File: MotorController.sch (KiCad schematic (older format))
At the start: 0 parts

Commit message: Added power, touch, and motor controller
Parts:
- added C? (x2): .1uF, symbol C
- added C? (x2): C, symbol C
- added M? (x4): Motor_DC, symbol Motor_DC
- added R? (x6): 10k, symbol R
- added U? (x2): A3916, symbol A3916
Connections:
- new net: M?.2 (-), U?.10 (OUT2B) (x2)
- new net: M?.2 (-), U?.12 (OUT1B) (x2)
- new net: R?.2, U?.13 (SENSE1) (x2)
- new net: M?.1 (+), U?.14 (OUT1A) (x2)
- new net: C?.1, U?.15 (VCP) (x2)
- new net: R?.1, U?.7 (FAULTn) (x2)
- new net: M?.1 (+), U?.8 (OUT2A) (x2)
- new net: R?.2, U?.9 (SENSE2) (x2)
- new net +5V: R?.2, R?.2
- new net 3V7: C?.1, C?.1, C?.2, C?.2, U?.11 (VBB), U?.11 (VBB)
- new net GND: C?.2, C?.2, R?.1, R?.1, R?.1, R?.1, U?.1 (GND), U?.1 (GND)
- new net MC1_IN1: U?.3 (IN1)
- new net MC1_IN2: U?.4 (IN2)
- new net MC1_IN3: U?.5 (IN3)
- new net MC1_IN4: U?.6 (IN4)
- new net MC1_SLEEPn: U?.2 (SLEEPn)
- new net MC2_IN1: U?.3 (IN1)
- new net MC2_IN2: U?.4 (IN2)
- new net MC2_IN3: U?.5 (IN3)
- new net MC2_IN4: U?.6 (IN4)
- new net MC2_SLEEPn: U?.2 (SLEEPn)

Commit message: Adding IR Sensor
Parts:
- gave numbers to parts that had none: 16
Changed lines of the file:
@@
 $EndDescr
 $Comp
-L A3916 U?
+L A3916 U1
 U 1 1 5AA4F077
 P 3775 3850
-F 0 "U?" H 3775 3750 60  0000 C CNN
+F 0 "U1" H 3775 3750 60  0000 C CNN
 F 1 "A3916" H 3775 3950 60  0000 C CNN
 F 2 "" H 3775 3850 60  0001 C CNN
@@
 MC1_IN4
 $Comp
-L R R?
+L R R1
 U 1 1 5AA4F12C
 P 2925 4100
-F 0 "R?" V 3005 4100 50  0000 C CNN
+F 0 "R1" V 3005 4100 50  0000 C CNN
 F 1 "10k" V 2925 4100 50  0000 C CNN
 F 2 "" V 2855 4100 50  0001 C CNN
@@
 $EndComp
 $Comp
-L +5V #PWR?
+L +5V #PWR01
 U 1 1 5AA4F16D
 P 2475 4100
-F 0 "#PWR?" H 2475 3950 50  0001 C CNN
+F 0 "#PWR01" H 2475 3950 50  0001 C CNN
 F 1 "+5V" H 2475 4240 50  0000 C CNN
 F 2 "" H 2475 4100 50  0001 C CNN
@@
 	2475 4100 2775 4100
 $Comp
-L GND #PWR?
+L GND #PWR02
 U 1 1 5AA4F189
 P 3075 4200
-F 0 "#PWR?" H 3075 3950 50  0001 C CNN
+F 0 "#PWR02" H 3075 3950 50  0001 C CNN
 F 1 "GND" H 3075 4050 50  0000 C CNN
 F 2 "" H 3075 4200 50  0001 C CNN
@@
 $EndComp
 $Comp
-L C C?
+L C C1
 U 1 1 5AA4F1A9
 P 4675 3450
-F 0 "C?" H 4700 3550 50  0000 L CNN
+F 0 "C1" H 4700 3550 50  0000 L CNN
 F 1 ".1uF" H 4700 3350 50  0000 L CNN
 F 2 "" H 4713 3300 50  0001 C CNN
@@
 Connection ~ 4675 3600
 $Comp
-L C C?
+L C C2
 U 1 1 5AA5030C
 P 5100 3450
-F 0 "C?" H 5125 3550 50  0000 L CNN
+F 0 "C2" H 5125 3550 50  0000 L CNN
 F 1 "C" H 5125 3350 50  0000 L CNN
 F 2 "" H 5138 3300 50  0001 C CNN
@@
 $EndComp
 $Comp
-L GND #PWR?
+L GND #PWR03
 U 1 1 5AA5037F
 P 5325 3300
-F 0 "#PWR?" H 5325 3050 50  0001 C CNN
+F 0 "#PWR03" H 5325 3050 50  0001 C CNN
 F 1 "GND" H 5325 3150 50  0000 C CNN
 F 2 "" H 5325 3300 50  0001 C CNN
@@
 	5100 3300 5325 3300
 $Comp
-L Motor_DC M?
+L Motor_DC M1
 U 1 1 5AA50637
 P 5100 3900
-F 0 "M?" H 5200 4000 50  0000 L CNN
+F 0 "M1" H 5200 4000 50  0000 L CNN
 F 1 "Motor_DC" H 5200 3700 50  0000 L TNN
 F 2 "" H 5100 3810 50  0001 C CNN
@@
 $EndComp
 $Comp
-L Motor_DC M?
+L Motor_DC M2
 U 1 1 5AA506D8
 P 5100 4500
-F 0 "M?" H 5200 4600 50  0000 L CNN
+F 0 "M2" H 5200 4600 50  0000 L CNN
 F 1 "Motor_DC" H 5200 4300 50  0000 L TNN
 F 2 "" H 5100 4410 50  0001 C CNN
@@
 	4900 4200 5100 4200
 $Comp
-L R R?
+L R R3
 U 1 1 5AA50734
 P 4625 3900
-F 0 "R?" V 4705 3900 50  0000 C CNN
+F 0 "R3" V 4705 3900 50  0000 C CNN
 F 1 "10k" V 4625 3900 50  0000 C CNN
 F 2 "" V 4555 3900 50  0001 C CNN
@@
 $EndComp
 $Comp
-L GND #PWR?
+L GND #PWR04
 U 1 1 5AA5078D
 P 4775 3900
-F 0 "#PWR?" H 4775 3650 50  0001 C CNN
+F 0 "#PWR04" H 4775 3650 50  0001 C CNN
 F 1 "GND" H 4775 3750 50  0000 C CNN
 F 2 "" H 4775 3900 50  0001 C CNN
@@
 	4625 4800 5100 4800
 $Comp
-L R R?
+L R R2
 U 1 1 5AA507E1
 P 4475 4350
-F 0 "R?" V 4555 4350 50  0000 C CNN
+F 0 "R2" V 4555 4350 50  0000 C CNN
 F 1 "10k" V 4475 4350 50  0000 C CNN
 F 2 "" V 4405 4350 50  0001 C CNN
@@
 $EndComp
 $Comp
-L GND #PWR?
+L GND #PWR05
 U 1 1 5AA5082F
 P 4475 4500
-F 0 "#PWR?" H 4475 4250 50  0001 C CNN
+F 0 "#PWR05" H 4475 4250 50  0001 C CNN
 F 1 "GND" H 4475 4350 50  0000 C CNN
 F 2 "" H 4475 4500 50  0001 C CNN
@@
 $EndComp
 $Comp
-L A3916 U?
+L A3916 U2
 U 1 1 5AA50C8A
 P 7625 3825
-F 0 "U?" H 7625 3725 60  0000 C CNN
+F 0 "U2" H 7625 3725 60  0000 C CNN
 F 1 "A3916" H 7625 3925 60  0000 C CNN
 F 2 "" H 7625 3825 60  0001 C CNN
@@
 MC2_IN4
 $Comp
-L R R?
+L R R4
 U 1 1 5AA50C95
 P 6775 4075
-F 0 "R?" V 6855 4075 50  0000 C CNN
+F 0 "R4" V 6855 4075 50  0000 C CNN
 F 1 "10k" V 6775 4075 50  0000 C CNN
 F 2 "" V 6705 4075 50  0001 C CNN
@@
 $EndComp
 $Comp
-L +5V #PWR?
+L +5V #PWR06
 U 1 1 5AA50C9B
 P 6325 4075
-F 0 "#PWR?" H 6325 3925 50  0001 C CNN
+F 0 "#PWR06" H 6325 3925 50  0001 C CNN
 F 1 "+5V" H 6325 4215 50  0000 C CNN
 F 2 "" H 6325 4075 50  0001 C CNN
@@
 	6325 4075 6625 4075
 $Comp
-L GND #PWR?
+L GND #PWR07
 U 1 1 5AA50CA2
 P 6925 4175
-F 0 "#PWR?" H 6925 3925 50  0001 C CNN
+F 0 "#PWR07" H 6925 3925 50  0001 C CNN
 F 1 "GND" H 6925 4025 50  0000 C CNN
 F 2 "" H 6925 4175 50  0001 C CNN
@@
 $EndComp
 $Comp
-L C C?
+L C C3
 U 1 1 5AA50CA8
 P 8525 3425
-F 0 "C?" H 8550 3525 50  0000 L CNN
+F 0 "C3" H 8550 3525 50  0000 L CNN
 F 1 ".1uF" H 8550 3325 50  0000 L CNN
 F 2 "" H 8563 3275 50  0001 C CNN
@@
 Connection ~ 8525 3575
 $Comp
-L C C?
+L C C4
 U 1 1 5AA50CB2
 P 8950 3425
-F 0 "C?" H 8975 3525 50  0000 L CNN
+F 0 "C4" H 8975 3525 50  0000 L CNN
 F 1 "C" H 8975 3325 50  0000 L CNN
 F 2 "" H 8988 3275 50  0001 C CNN
@@
 $EndComp
 $Comp
-L GND #PWR?
+L GND #PWR08
 U 1 1 5AA50CB8
 P 9175 3275
-F 0 "#PWR?" H 9175 3025 50  0001 C CNN
+F 0 "#PWR08" H 9175 3025 50  0001 C CNN
 F 1 "GND" H 9175 3125 50  0000 C CNN
 F 2 "" H 9175 3275 50  0001 C CNN
@@
 	8950 3275 9175 3275
 $Comp
-L Motor_DC M?
+L Motor_DC M3
 U 1 1 5AA50CC1
 P 8950 3875
-F 0 "M?" H 9050 3975 50  0000 L CNN
+F 0 "M3" H 9050 3975 50  0000 L CNN
 F 1 "Motor_DC" H 9050 3675 50  0000 L TNN
 F 2 "" H 8950 3785 50  0001 C CNN
@@
 $EndComp
 $Comp
-L Motor_DC M?
+L Motor_DC M4
 U 1 1 5AA50CC7
 P 8950 4475
-F 0 "M?" H 9050 4575 50  0000 L CNN
+F 0 "M4" H 9050 4575 50  0000 L CNN
 F 1 "Motor_DC" H 9050 4275 50  0000 L TNN
 F 2 "" H 8950 4385 50  0001 C CNN
@@
 	8750 4175 8950 4175
 $Comp
-L R R?
+L R R6
 U 1 1 5AA50CD1
 P 8475 3875
-F 0 "R?" V 8555 3875 50  0000 C CNN
+F 0 "R6" V 8555 3875 50  0000 C CNN
 F 1 "10k" V 8475 3875 50  0000 C CNN
 F 2 "" V 8405 3875 50  0001 C CNN
@@
 $EndComp
 $Comp
-L GND #PWR?
+L GND #PWR09
 U 1 1 5AA50CD7
 P 8625 3875
-F 0 "#PWR?" H 8625 3625 50  0001 C CNN
+F 0 "#PWR09" H 8625 3625 50  0001 C CNN
 F 1 "GND" H 8625 3725 50  0000 C CNN
 F 2 "" H 8625 3875 50  0001 C CNN
@@
 	8475 4775 8950 4775
 $Comp
-L R R?
+L R R5
 U 1 1 5AA50CE3
 P 8325 4325
-F 0 "R?" V 8405 4325 50  0000 C CNN
+F 0 "R5" V 8405 4325 50  0000 C CNN
 F 1 "10k" V 8325 4325 50  0000 C CNN
 F 2 "" V 8255 4325 50  0001 C CNN
@@
 $EndComp
 $Comp
-L GND #PWR?
+L GND #PWR010
 U 1 1 5AA50CE9
 P 8325 4475
-F 0 "#PWR?" H 8325 4225 50  0001 C CNN
+F 0 "#PWR010" H 8325 4225 50  0001 C CNN
 F 1 "GND" H 8325 4325 50  0000 C CNN
 F 2 "" H 8325 4475 50  0001 C CNN

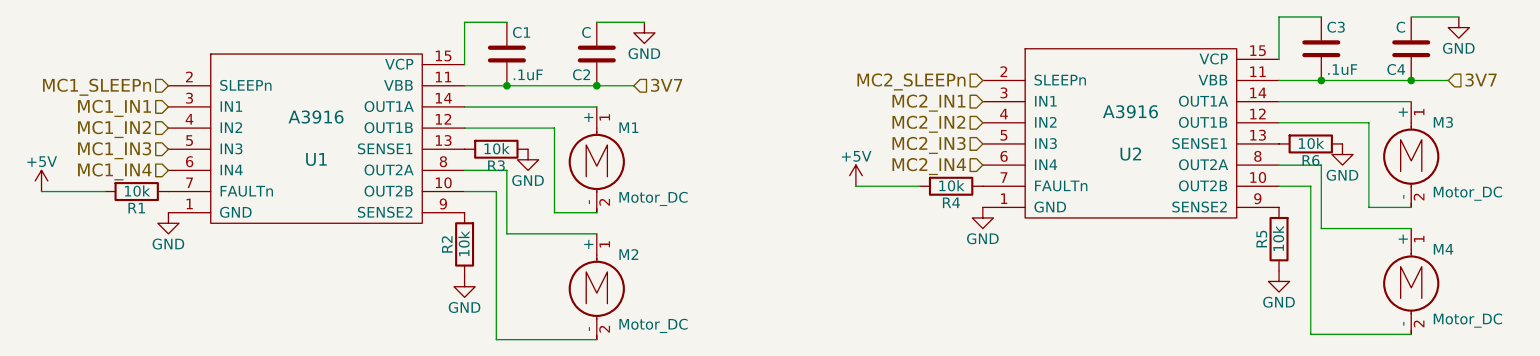
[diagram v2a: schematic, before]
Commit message: Started associating footprints
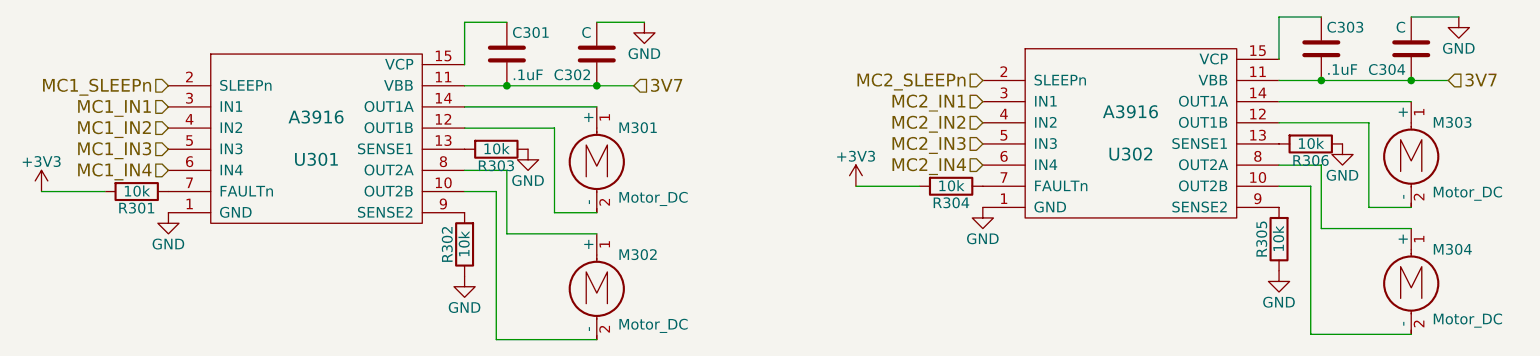
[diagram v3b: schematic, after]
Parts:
- C301: renamed from C1; footprint (none) -> Capacitors_SMD:C_0402
- C303: renamed from C3; footprint (none) -> Capacitors_SMD:C_0402
- renumbered C2 to C302, C4 to C304, M1 to M301, M2 to M302, M3 to M303, M4 to M304, R1 to R301, R2 to R302, R3 to R303, R4 to R304, R5 to R305, R6 to R306, U1 to U301, U2 to U302
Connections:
- net +5V renamed +3V3
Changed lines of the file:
@@
 $EndDescr
 $Comp
-L A3916 U1
+L A3916 U301
 U 1 1 5AA4F077
 P 3775 3850
-F 0 "U1" H 3775 3750 60  0000 C CNN
+F 0 "U301" H 3775 3750 60  0000 C CNN
 F 1 "A3916" H 3775 3950 60  0000 C CNN
 F 2 "" H 3775 3850 60  0001 C CNN
@@
 MC1_IN4
 $Comp
-L R R1
+L R R301
 U 1 1 5AA4F12C
 P 2925 4100
-F 0 "R1" V 3005 4100 50  0000 C CNN
+F 0 "R301" V 3005 4100 50  0000 C CNN
 F 1 "10k" V 2925 4100 50  0000 C CNN
 F 2 "" V 2855 4100 50  0001 C CNN
@@
 	0    1    1    0
 $EndComp
-$Comp
-L +5V #PWR01
-U 1 1 5AA4F16D
-P 2475 4100
-F 0 "#PWR01" H 2475 3950 50  0001 C CNN
-F 1 "+5V" H 2475 4240 50  0000 C CNN
-F 2 "" H 2475 4100 50  0001 C CNN
-F 3 "" H 2475 4100 50  0001 C CNN
-	1    2475 4100
-	1    0    0    -1
-$EndComp
 Wire Wire Line
 	2475 4100 2775 4100
 $Comp
-L GND #PWR02
+L GND #PWR013
 U 1 1 5AA4F189
 P 3075 4200
-F 0 "#PWR02" H 3075 3950 50  0001 C CNN
+F 0 "#PWR013" H 3075 3950 50  0001 C CNN
 F 1 "GND" H 3075 4050 50  0000 C CNN
 F 2 "" H 3075 4200 50  0001 C CNN
@@
 $EndComp
 $Comp
-L C C1
+L C C301
 U 1 1 5AA4F1A9
 P 4675 3450
-F 0 "C1" H 4700 3550 50  0000 L CNN
+F 0 "C301" H 4700 3550 50  0000 L CNN
 F 1 ".1uF" H 4700 3350 50  0000 L CNN
-F 2 "" H 4713 3300 50  0001 C CNN
+F 2 "Capacitors_SMD:C_0402" H 4713 3300 50  0001 C CNN
 F 3 "" H 4675 3450 50  0001 C CNN
 	1    4675 3450
@@
 Connection ~ 4675 3600
 $Comp
-L C C2
+L C C302
 U 1 1 5AA5030C
 P 5100 3450
-F 0 "C2" H 5125 3550 50  0000 L CNN
+F 0 "C302" H 5125 3550 50  0000 L CNN
 F 1 "C" H 5125 3350 50  0000 L CNN
 F 2 "" H 5138 3300 50  0001 C CNN
@@
 $EndComp
 $Comp
-L GND #PWR03
+L GND #PWR014
 U 1 1 5AA5037F
 P 5325 3300
-F 0 "#PWR03" H 5325 3050 50  0001 C CNN
+F 0 "#PWR014" H 5325 3050 50  0001 C CNN
 F 1 "GND" H 5325 3150 50  0000 C CNN
 F 2 "" H 5325 3300 50  0001 C CNN
@@
 	5100 3300 5325 3300
 $Comp
-L Motor_DC M1
+L Motor_DC M301
 U 1 1 5AA50637
 P 5100 3900
-F 0 "M1" H 5200 4000 50  0000 L CNN
+F 0 "M301" H 5200 4000 50  0000 L CNN
 F 1 "Motor_DC" H 5200 3700 50  0000 L TNN
 F 2 "" H 5100 3810 50  0001 C CNN
@@
 $EndComp
 $Comp
-L Motor_DC M2
+L Motor_DC M302
 U 1 1 5AA506D8
 P 5100 4500
-F 0 "M2" H 5200 4600 50  0000 L CNN
+F 0 "M302" H 5200 4600 50  0000 L CNN
 F 1 "Motor_DC" H 5200 4300 50  0000 L TNN
 F 2 "" H 5100 4410 50  0001 C CNN
@@
 	4900 4200 5100 4200
 $Comp
-L R R3
+L R R303
 U 1 1 5AA50734
 P 4625 3900
-F 0 "R3" V 4705 3900 50  0000 C CNN
+F 0 "R303" V 4705 3900 50  0000 C CNN
 F 1 "10k" V 4625 3900 50  0000 C CNN
 F 2 "" V 4555 3900 50  0001 C CNN
@@
 $EndComp
 $Comp
-L GND #PWR04
+L GND #PWR015
 U 1 1 5AA5078D
 P 4775 3900
-F 0 "#PWR04" H 4775 3650 50  0001 C CNN
+F 0 "#PWR015" H 4775 3650 50  0001 C CNN
 F 1 "GND" H 4775 3750 50  0000 C CNN
 F 2 "" H 4775 3900 50  0001 C CNN
@@
 	4625 4800 5100 4800
 $Comp
-L R R2
+L R R302
 U 1 1 5AA507E1
 P 4475 4350
-F 0 "R2" V 4555 4350 50  0000 C CNN
+F 0 "R302" V 4555 4350 50  0000 C CNN
 F 1 "10k" V 4475 4350 50  0000 C CNN
 F 2 "" V 4405 4350 50  0001 C CNN
@@
 $EndComp
 $Comp
-L GND #PWR05
+L GND #PWR016
 U 1 1 5AA5082F
 P 4475 4500
-F 0 "#PWR05" H 4475 4250 50  0001 C CNN
+F 0 "#PWR016" H 4475 4250 50  0001 C CNN
 F 1 "GND" H 4475 4350 50  0000 C CNN
 F 2 "" H 4475 4500 50  0001 C CNN
@@
 $EndComp
 $Comp
-L A3916 U2
+L A3916 U302
 U 1 1 5AA50C8A
 P 7625 3825
-F 0 "U2" H 7625 3725 60  0000 C CNN
+F 0 "U302" H 7625 3725 60  0000 C CNN
 F 1 "A3916" H 7625 3925 60  0000 C CNN
 F 2 "" H 7625 3825 60  0001 C CNN
@@
 MC2_IN4
 $Comp
-L R R4
+L R R304
 U 1 1 5AA50C95
 P 6775 4075
-F 0 "R4" V 6855 4075 50  0000 C CNN
+F 0 "R304" V 6855 4075 50  0000 C CNN
 F 1 "10k" V 6775 4075 50  0000 C CNN
 F 2 "" V 6705 4075 50  0001 C CNN
@@
 	0    1    1    0
 $EndComp
-$Comp
-L +5V #PWR06
-U 1 1 5AA50C9B
-P 6325 4075
-F 0 "#PWR06" H 6325 3925 50  0001 C CNN
-F 1 "+5V" H 6325 4215 50  0000 C CNN
-F 2 "" H 6325 4075 50  0001 C CNN
-F 3 "" H 6325 4075 50  0001 C CNN
-	1    6325 4075
-	1    0    0    -1
-$EndComp
 Wire Wire Line
 	6325 4075 6625 4075
 $Comp
-L GND #PWR07
+L GND #PWR017
 U 1 1 5AA50CA2
 P 6925 4175
-F 0 "#PWR07" H 6925 3925 50  0001 C CNN
+F 0 "#PWR017" H 6925 3925 50  0001 C CNN
 F 1 "GND" H 6925 4025 50  0000 C CNN
 F 2 "" H 6925 4175 50  0001 C CNN
@@
 $EndComp
 $Comp
-L C C3
+L C C303
 U 1 1 5AA50CA8
 P 8525 3425
-F 0 "C3" H 8550 3525 50  0000 L CNN
+F 0 "C303" H 8550 3525 50  0000 L CNN
 F 1 ".1uF" H 8550 3325 50  0000 L CNN
-F 2 "" H 8563 3275 50  0001 C CNN
+F 2 "Capacitors_SMD:C_0402" H 8563 3275 50  0001 C CNN
 F 3 "" H 8525 3425 50  0001 C CNN
 	1    8525 3425
@@
 Connection ~ 8525 3575
 $Comp
-L C C4
+L C C304
 U 1 1 5AA50CB2
 P 8950 3425
-F 0 "C4" H 8975 3525 50  0000 L CNN
+F 0 "C304" H 8975 3525 50  0000 L CNN
 F 1 "C" H 8975 3325 50  0000 L CNN
 F 2 "" H 8988 3275 50  0001 C CNN
@@
 $EndComp
 $Comp
-L GND #PWR08
+L GND #PWR018
 U 1 1 5AA50CB8
 P 9175 3275
-F 0 "#PWR08" H 9175 3025 50  0001 C CNN
+F 0 "#PWR018" H 9175 3025 50  0001 C CNN
 F 1 "GND" H 9175 3125 50  0000 C CNN
 F 2 "" H 9175 3275 50  0001 C CNN
@@
 	8950 3275 9175 3275
 $Comp
-L Motor_DC M3
+L Motor_DC M303
 U 1 1 5AA50CC1
 P 8950 3875
-F 0 "M3" H 9050 3975 50  0000 L CNN
+F 0 "M303" H 9050 3975 50  0000 L CNN
 F 1 "Motor_DC" H 9050 3675 50  0000 L TNN
 F 2 "" H 8950 3785 50  0001 C CNN
@@
 $EndComp
 $Comp
-L Motor_DC M4
+L Motor_DC M304
 U 1 1 5AA50CC7
 P 8950 4475
-F 0 "M4" H 9050 4575 50  0000 L CNN
+F 0 "M304" H 9050 4575 50  0000 L CNN
 F 1 "Motor_DC" H 9050 4275 50  0000 L TNN
 F 2 "" H 8950 4385 50  0001 C CNN
@@
 	8750 4175 8950 4175
 $Comp
-L R R6
+L R R306
 U 1 1 5AA50CD1
 P 8475 3875
-F 0 "R6" V 8555 3875 50  0000 C CNN
+F 0 "R306" V 8555 3875 50  0000 C CNN
 F 1 "10k" V 8475 3875 50  0000 C CNN
 F 2 "" V 8405 3875 50  0001 C CNN
@@
 $EndComp
 $Comp
-L GND #PWR09
+L GND #PWR019
 U 1 1 5AA50CD7
 P 8625 3875
-F 0 "#PWR09" H 8625 3625 50  0001 C CNN
+F 0 "#PWR019" H 8625 3625 50  0001 C CNN
 F 1 "GND" H 8625 3725 50  0000 C CNN
 F 2 "" H 8625 3875 50  0001 C CNN
@@
 	8475 4775 8950 4775
 $Comp
-L R R5
+L R R305
 U 1 1 5AA50CE3
 P 8325 4325
-F 0 "R5" V 8405 4325 50  0000 C CNN
+F 0 "R305" V 8405 4325 50  0000 C CNN
 F 1 "10k" V 8325 4325 50  0000 C CNN
 F 2 "" V 8255 4325 50  0001 C CNN
@@
 $EndComp
 $Comp
-L GND #PWR010
+L GND #PWR020
 U 1 1 5AA50CE9
 P 8325 4475
-F 0 "#PWR010" H 8325 4225 50  0001 C CNN
+F 0 "#PWR020" H 8325 4225 50  0001 C CNN
 F 1 "GND" H 8325 4325 50  0000 C CNN
 F 2 "" H 8325 4475 50  0001 C CNN
@@
 	1    0    0    -1
 $EndComp
+$Comp
+L +3V3 #PWR021
+U 1 1 5AC691BA
+P 2475 4100
+F 0 "#PWR021" H 2475 3950 50  0001 C CNN
+F 1 "+3V3" H 2475 4240 50  0000 C CNN
+F 2 "" H 2475 4100 50  0001 C CNN
+F 3 "" H 2475 4100 50  0001 C CNN
+	1    2475 4100
+	1    0    0    -1
+$EndComp
+$Comp
+L +3V3 #PWR022
+U 1 1 5AC693DE
+P 6325 4075
+F 0 "#PWR022" H 6325 3925 50  0001 C CNN
+F 1 "+3V3" H 6325 4215 50  0000 C CNN
+F 2 "" H 6325 4075 50  0001 C CNN
+F 3 "" H 6325 4075 50  0001 C CNN
+	1    6325 4075
+	1    0    0    -1
+$EndComp
